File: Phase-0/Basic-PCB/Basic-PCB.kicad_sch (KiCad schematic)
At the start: 28 parts, among them J1 Flexor Digitorum Superficialis, J2 Flexor Carpi Radialis, J3 output, J4 Conn_01x02, U1 LM358, U2 LM358, U3 LM358

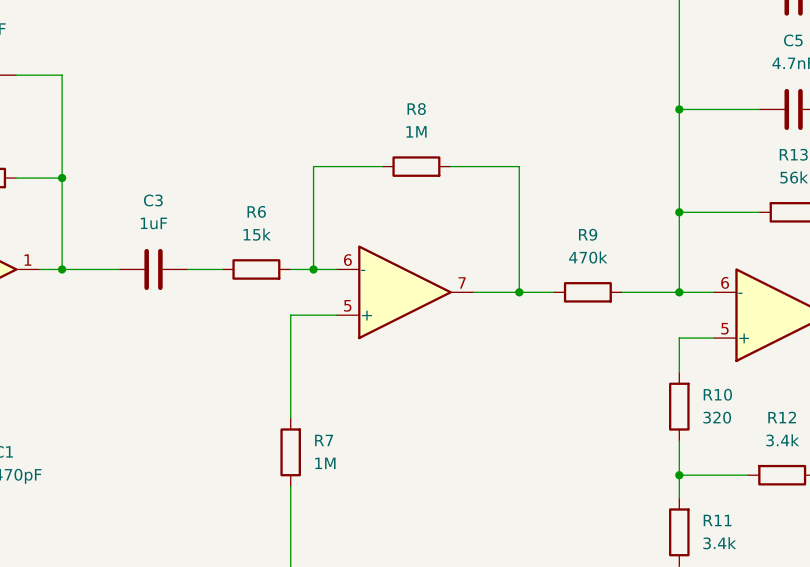
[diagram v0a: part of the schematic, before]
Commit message: Improved Phase 0 PCB
Made slightly more compact PCB and include op amp models
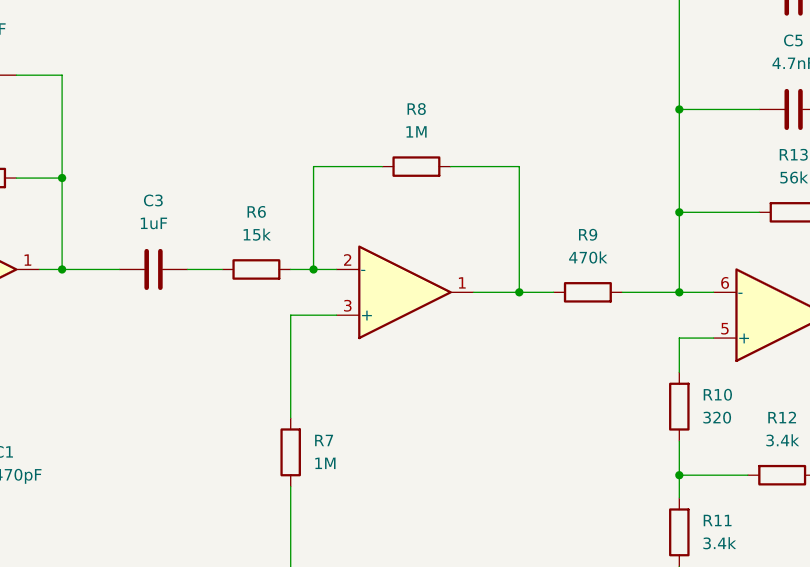
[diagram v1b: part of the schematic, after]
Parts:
- renumbered U2 to U3
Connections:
- net at R6.2, R8.1: now also U3.2 (-); no longer U3.6 (-)
- net at R8.2, R9.1: now also U3.1; no longer U3.7
- net at R7.2: now also U3.3 (+); no longer U3.5 (+)
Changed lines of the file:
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@@
-			)
-		)
-		(property "Field5" ""
-			(at 104.14 161.29 0)
-			(effects
-				(font
-					(size 1.27 1.27)
-				)
-				(hide yes)
 			)
 		)
@@
 		(at 158.75 100.33 0)
 		(mirror x)
-		(unit 2)
-		(exclude_from_sim no)
-		(in_bom yes)
-		(on_board yes)
-		(dnp no)
-		(property "Reference" "U2"
+		(unit 1)
+		(exclude_from_sim no)
+		(in_bom yes)
+		(on_board yes)
+		(dnp no)
+		(property "Reference" "U3"
 			(at 158.75 110.49 0)
 			(effects
@@
 			(project "Basic-PCB"
 				(path "/3a549d42-e461-4510-ac41-c51a5743c9d2"
-					(reference "U2")
-					(unit 2)
+					(reference "U3")
+					(unit 1)
 				)
 			)
@@
 			(at 200.66 102.87 0)
 			(effects
-				(font
-					(size 1.27 1.27)
-				)
-				(hide yes)
-			)
-		)
-		(property "Field5" ""
-			(at 200.66 102.87 0)
-			(effects

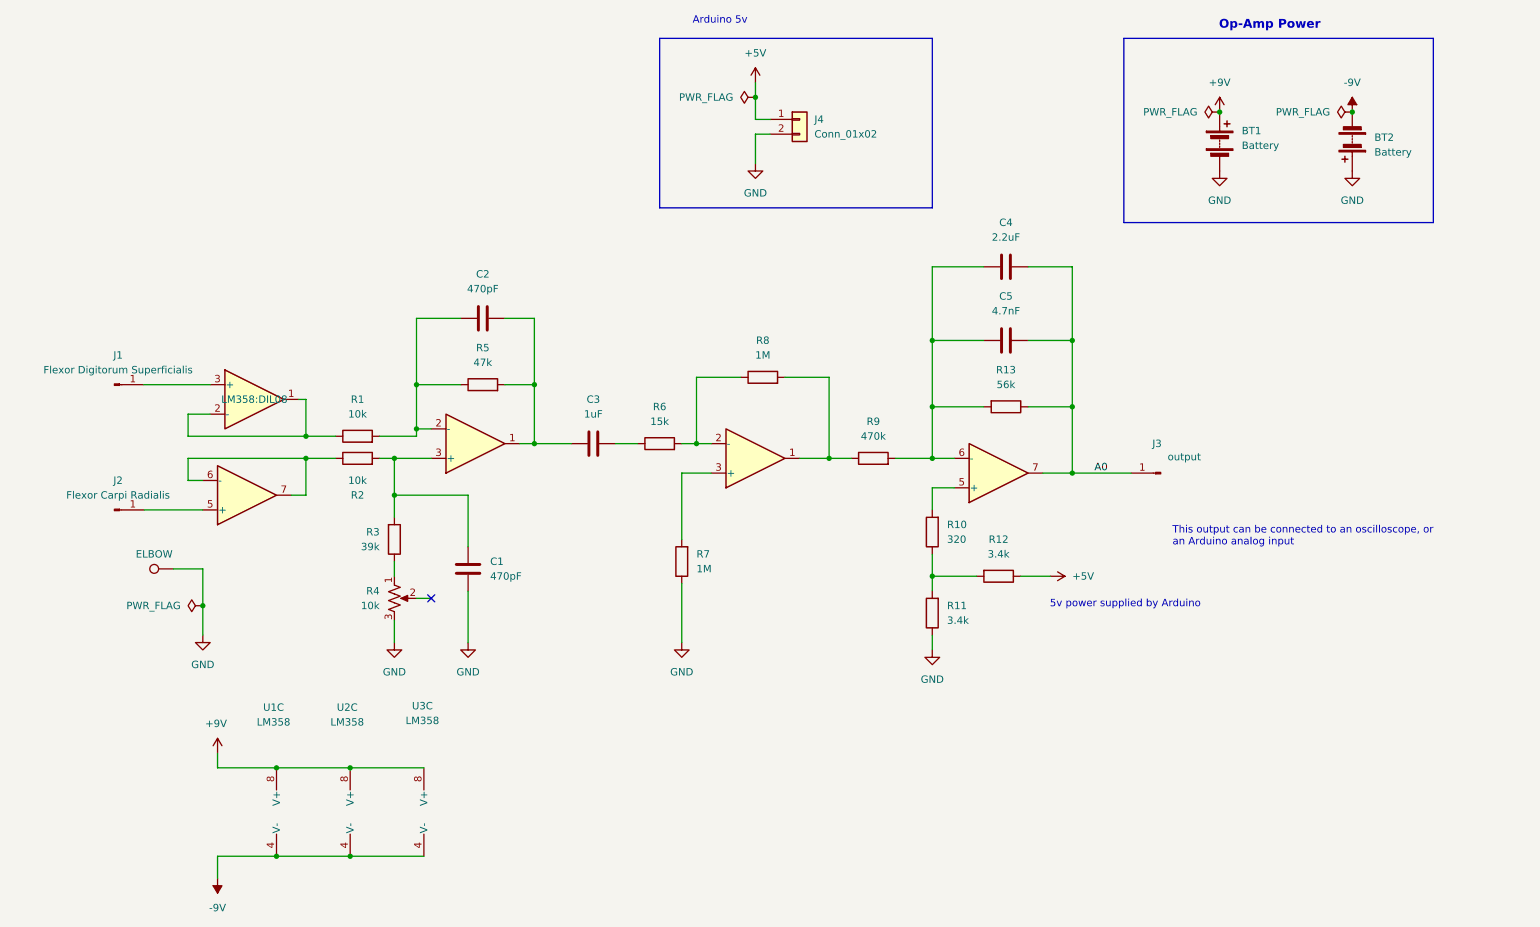
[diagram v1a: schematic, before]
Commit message: Changed footprints for battery terminals
Changed footprints for battery terminals to ones found in a Makerspace nearby
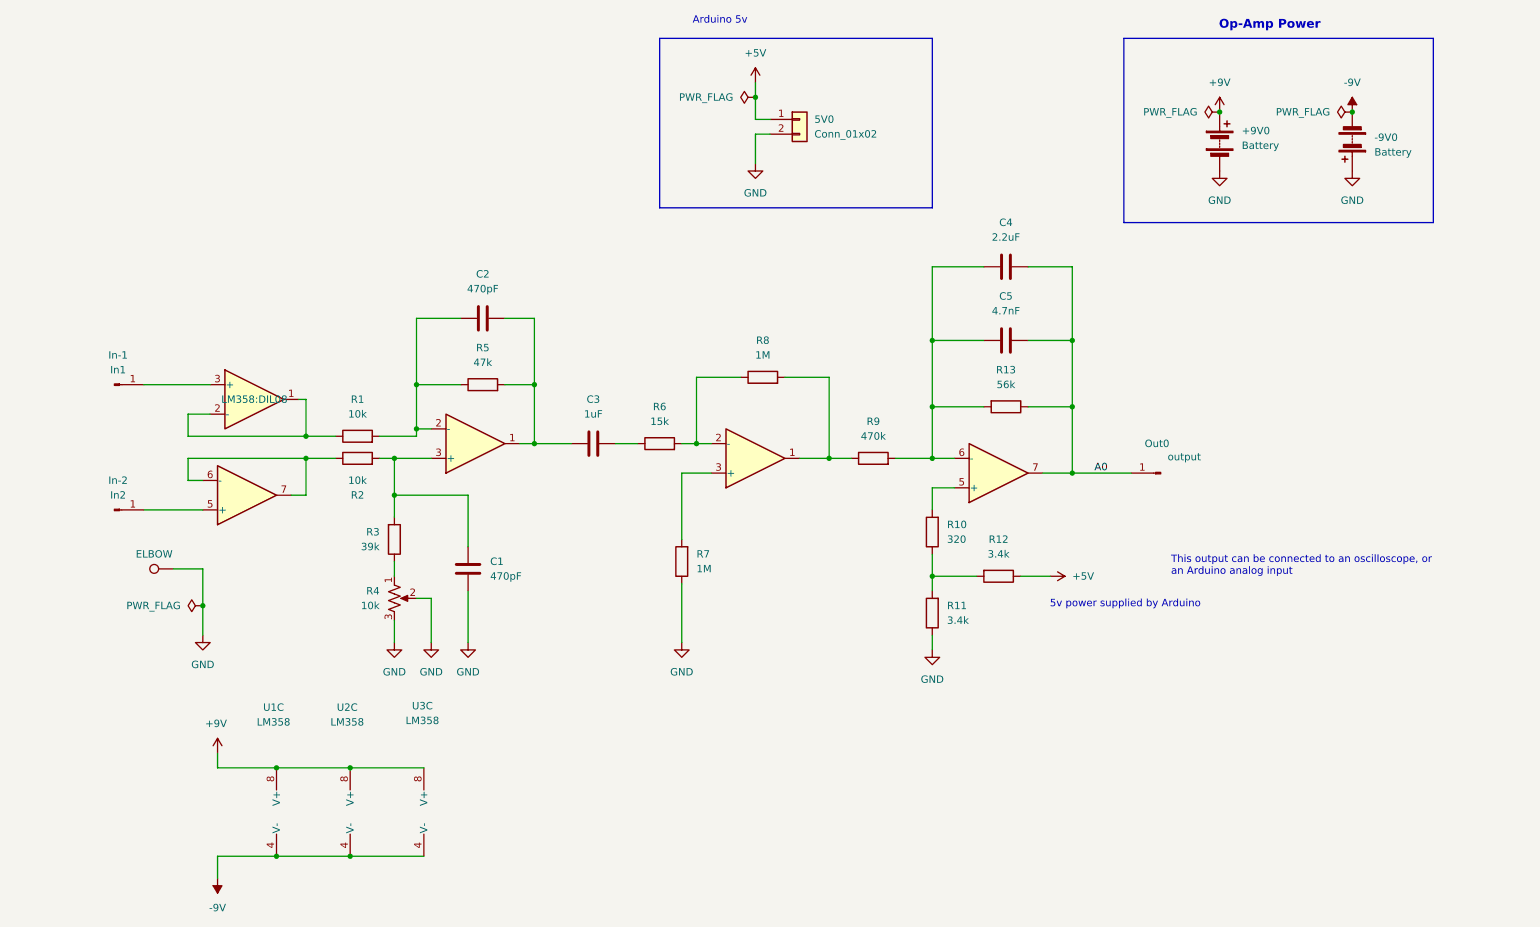
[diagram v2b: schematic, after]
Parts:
- 5V0: renamed from J4; footprint Connector_PinSocket_1.00mm:PinSocket_1x02_P1.00mm_Vertical -> Connector_PinSocket_2.54mm:PinSocket_1x02_P2.54mm_Vertical
- Elbow: renamed from TP1; footprint TestPoint:TestPoint_Bridge_Pitch3.81mm_Drill1.3mm -> TestPoint:TestPoint_Keystone_5000-5004_Miniature
- In-1: renamed from J1; value Flexor Digitorum Superficialis -> In1; footprint TestPoint:TestPoint_Bridge_Pitch3.81mm_Drill1.3mm -> TestPoint:TestPoint_Keystone_5000-5004_Miniature
- In-2: renamed from J2; value Flexor Carpi Radialis -> In2; footprint TestPoint:TestPoint_Bridge_Pitch3.81mm_Drill1.3mm -> TestPoint:TestPoint_Keystone_5000-5004_Miniature
- Out0: renamed from J3; footprint TestPoint:TestPoint_Bridge_Pitch3.81mm_Drill1.3mm -> TestPoint:TestPoint_Keystone_5000-5004_Miniature
- R4: footprint Potentiometer_THT:Potentiometer_ACP_CA14-H2,5_Horizontal -> Potentiometer_THT:Potentiometer_Bourns_3006P_Horizontal
- renumbered BT1 to +9V0, BT2 to -9V0
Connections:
- net GND: now also R4.2
- no-connect marks 1 -> 0
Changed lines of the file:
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@@
 		(color 0 0 0 0)
 	)
-	(no_connect
-		(at 102.87 124.46)
+	(wire
+		(pts
+			(xy 100.33 124.46) (xy 102.87 124.46)
+		)
+		(stroke
+			(width 0)
+			(type default)
+		)
 	)
 	(wire
@@
 	(wire
 		(pts
-			(xy 100.33 124.46) (xy 102.87 124.46)
+			(xy 102.87 124.46) (xy 102.87 132.08)
 		)
 		(stroke
@@
 	(text "This output can be connected to an oscilloscope, or \nan Arduino analog input"
 		(exclude_from_sim no)
-		(at 230.632 113.792 0)
+		(at 230.378 118.872 0)
 		(effects
 			(font
@@
 		(dnp no)
 		(fields_autoplaced yes)
-		(property "Reference" "TP1"
+		(property "Reference" "Elbow"
 			(at 55.118 114.3 90)
 			(effects
@@
 			)
 		)
-		(property "Footprint" "TestPoint:TestPoint_Bridge_Pitch3.81mm_Drill1.3mm"
+		(property "Footprint" "TestPoint:TestPoint_Keystone_5000-5004_Miniature"
 			(at 58.42 114.3 0)
 			(effects
@@
 			(project "Basic-PCB"
 				(path "/3a549d42-e461-4510-ac41-c51a5743c9d2"
-					(reference "TP1")
+					(reference "Elbow")
 					(unit 1)
 				)
@@
 	)
 	(symbol
+		(lib_id "power:GND")
+		(at 102.87 132.08 0)
+		(unit 1)
+		(exclude_from_sim no)
+		(in_bom yes)
+		(on_board yes)
+		(dnp no)
+		(fields_autoplaced yes)
+		(property "Reference" "#PWR06"
+			(at 102.87 138.43 0)
+			(effects
+				(font
+					(size 1.27 1.27)
+				)
+				(hide yes)
+			)
+		)
+		(property "Value" "GND"
+			(at 102.87 137.16 0)
+			(effects
+				(font
+					(size 1.27 1.27)
+				)
+			)
+		)
+		(property "Footprint" ""
+			(at 102.87 132.08 0)
+			(effects
+				(font
+					(size 1.27 1.27)
+				)
+				(hide yes)
+			)
+		)
+		(property "Datasheet" ""
+			(at 102.87 132.08 0)
+			(effects
+				(font
+					(size 1.27 1.27)
+				)
+				(hide yes)
+			)
+		)
+		(property "Description" "Power symbol creates a global label with name \"GND\" , ground"
+			(at 102.87 132.08 0)
+			(effects
+				(font
+					(size 1.27 1.27)
+				)
+				(hide yes)
+			)
+		)
+		(pin "1"
+		)
+		(instances
+			(project ""
+				(path "/3a549d42-e461-4510-ac41-c51a5743c9d2"
+					(reference "#PWR06")
+					(unit 1)
+				)
+			)
+		)
+	)
+	(symbol
 		(lib_id "Device:Battery")
 		(at 261.62 45.72 180)
@@
 		(dnp no)
 		(fields_autoplaced yes)
-		(property "Reference" "BT2"
+		(property "Reference" "-9V0"
 			(at 265.43 45.0214 0)
 			(effects
@@
 			(project "Basic-PCB"
 				(path "/3a549d42-e461-4510-ac41-c51a5743c9d2"
-					(reference "BT2")
+					(reference "-9V0")
 					(unit 1)
 				)
@@
 		(dnp no)
 		(fields_autoplaced yes)
-		(property "Reference" "J1"
+		(property "Reference" "In-1"
 			(at 48.895 82.55 0)
 			(effects
@@
 			)
 		)
-		(property "Value" "Flexor Digitorum Superficialis"
+		(property "Value" "In1"
 			(at 48.895 85.09 0)
 			(effects
@@
 			)
 		)
-		(property "Footprint" "TestPoint:TestPoint_Bridge_Pitch3.81mm_Drill1.3mm"
+		(property "Footprint" "TestPoint:TestPoint_Keystone_5000-5004_Miniature"
 			(at 48.26 87.63 0)
 			(effects
@@
 			(project "Basic-PCB"
 				(path "/3a549d42-e461-4510-ac41-c51a5743c9d2"
-					(reference "J1")
+					(reference "In-1")
 					(unit 1)
 				)
@@
 		(dnp no)
 		(fields_autoplaced yes)
-		(property "Reference" "BT1"
+		(property "Reference" "+9V0"
 			(at 242.57 43.8784 0)
 			(effects
@@
 			(project "Basic-PCB"
 				(path "/3a549d42-e461-4510-ac41-c51a5743c9d2"
-					(reference "BT1")
+					(reference "+9V0")
 					(unit 1)
 				)
@@
 		(on_board yes)
 		(dnp no)
-		(property "Reference" "J3"
+		(property "Reference" "Out0"
 			(at 227.965 97.79 0)
 			(effects
@@
 			)
 		)
-		(property "Footprint" "TestPoint:TestPoint_Bridge_Pitch3.81mm_Drill1.3mm"
+		(property "Footprint" "TestPoint:TestPoint_Keystone_5000-5004_Miniature"
 			(at 228.6 102.87 0)
 			(effects
@@
 			(project ""
 				(path "/3a549d42-e461-4510-ac41-c51a5743c9d2"
-					(reference "J3")
+					(reference "Out0")
 					(unit 1)
 				)
@@
 			)
 		)
-		(property "Footprint" "Potentiometer_THT:Potentiometer_ACP_CA14-H2,5_Horizontal"
+		(property "Footprint" "Potentiometer_THT:Potentiometer_Bourns_3006P_Horizontal"
 			(at 96.52 124.46 0)
 			(effects
@@
 		(dnp no)
 		(fields_autoplaced yes)
-		(property "Reference" "J2"
+		(property "Reference" "In-2"
 			(at 48.895 104.14 0)
 			(effects
@@
 			)
 		)
-		(property "Value" "Flexor Carpi Radialis"
+		(property "Value" "In2"
 			(at 48.895 106.68 0)
 			(effects
@@
 			)
 		)
-		(property "Footprint" "TestPoint:TestPoint_Bridge_Pitch3.81mm_Drill1.3mm"
+		(property "Footprint" "TestPoint:TestPoint_Keystone_5000-5004_Miniature"
 			(at 48.26 109.22 0)
 			(effects
@@
 			(project "Basic-PCB"
 				(path "/3a549d42-e461-4510-ac41-c51a5743c9d2"
-					(reference "J2")
+					(reference "In-2")
 					(unit 1)
 				)
@@
 		(dnp no)
 		(fields_autoplaced yes)
-		(property "Reference" "J4"
+		(property "Reference" "5V0"
 			(at 168.91 41.9099 0)
 			(effects
@@
 			)
 		)
-		(property "Footprint" "Connector_PinSocket_1.00mm:PinSocket_1x02_P1.00mm_Vertical"
+		(property "Footprint" "Connector_PinSocket_2.54mm:PinSocket_1x02_P2.54mm_Vertical"
 			(at 166.37 41.91 0)
 			(effects
@@
 			(project ""
 				(path "/3a549d42-e461-4510-ac41-c51a5743c9d2"
-					(reference "J4")
+					(reference "5V0")
 					(unit 1)
 				)
